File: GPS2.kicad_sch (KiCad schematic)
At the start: 12 parts, among them J3 GPS_ANT_2, U4 NEO-6M-GPS, U5 24AA32A-I_ST

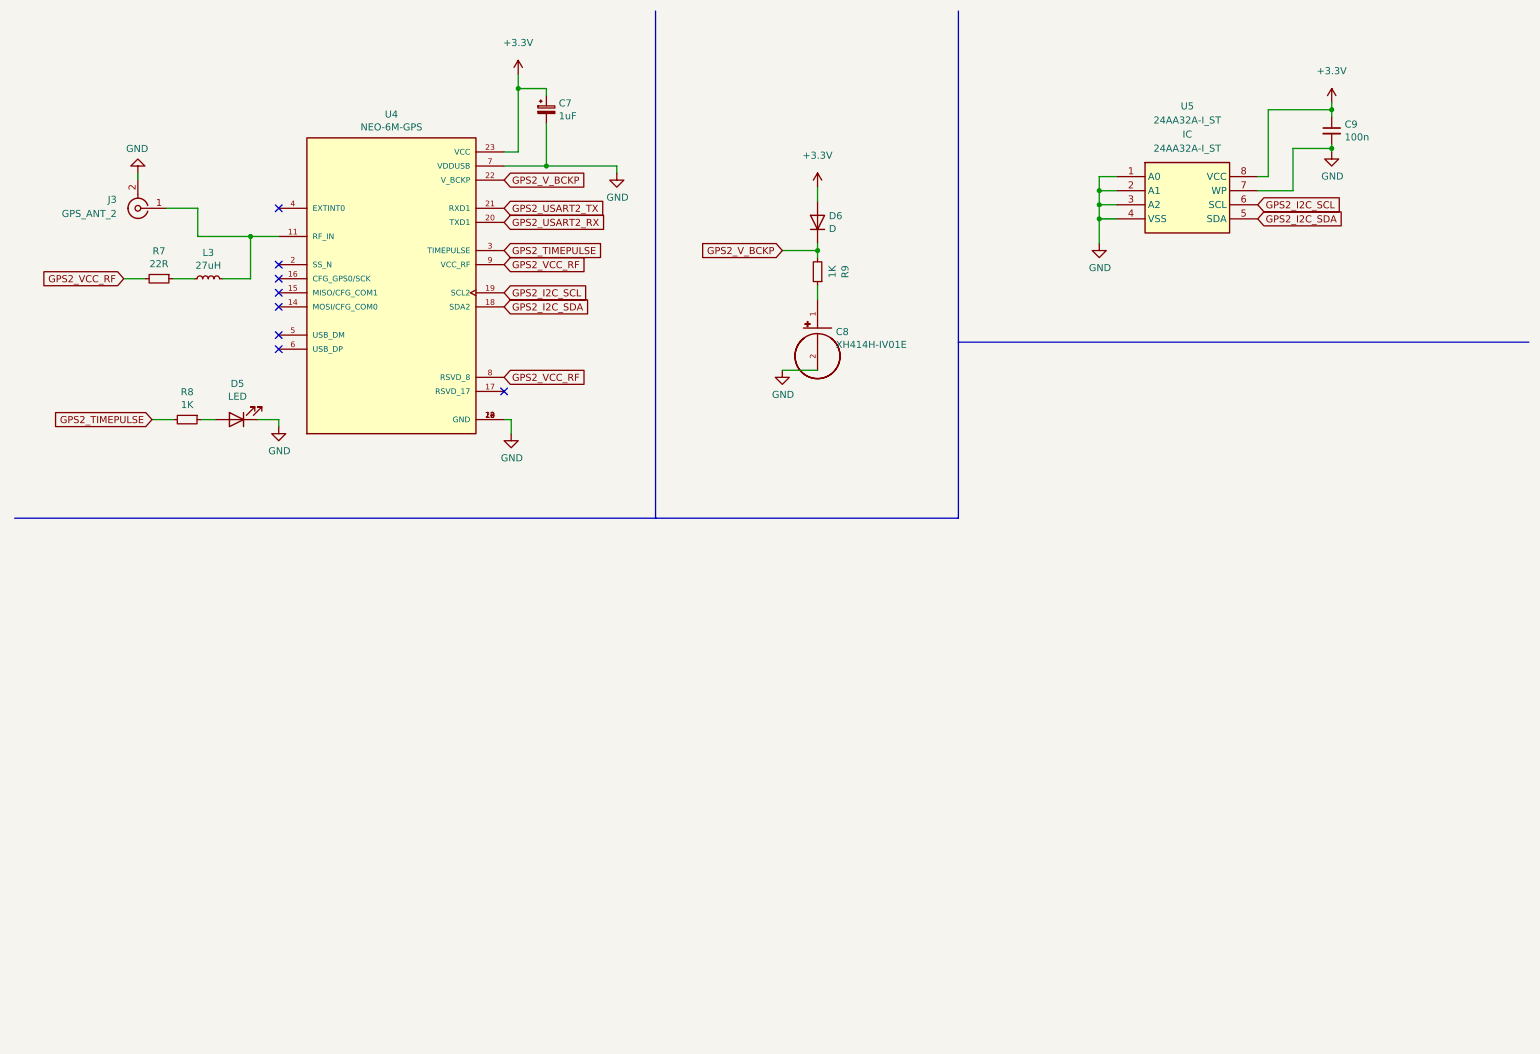
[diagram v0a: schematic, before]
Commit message: Adding M10
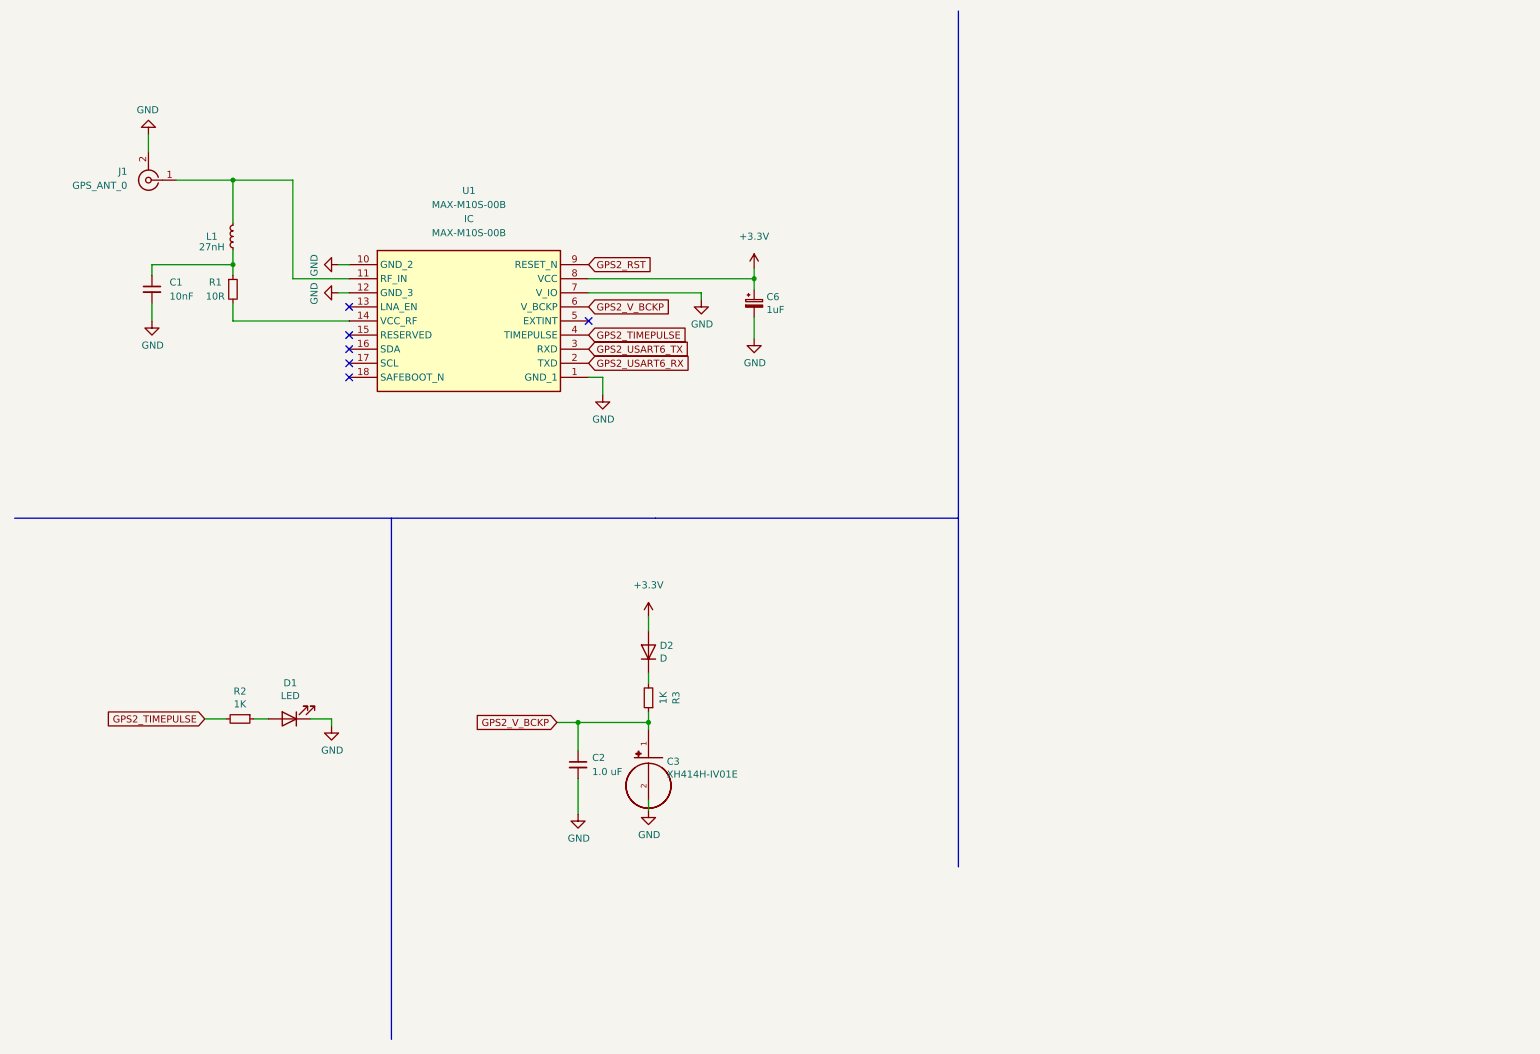
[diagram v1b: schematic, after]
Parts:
- removed C7: 1uF, Capacitor_Tantalum_SMD:CP_EIA-3528-21_Kemet-B_Pad1.50x2.35mm_HandSolder, symbol Device:CP_Small
- removed C8: XH414H-IV01E, XH414H:CAP_XH414H-IV01E, symbol XH414H-IV01E:XH414H-IV01E
- removed C9: 100n, Capacitor_SMD:C_0402_1005Metric, symbol Device:C_Small
- removed D5: LED, LED_SMD:LED_0805_2012Metric_Pad1.15x1.40mm_HandSolder, symbol Device:LED
- removed D6: D, Diode_SMD:D_1206_3216Metric_Pad1.42x1.75mm_HandSolder, symbol Device:D
- removed J3: GPS_ANT_2, Connector_Coaxial:SMA_Samtec_SMA-J-P-X-ST-EM1_EdgeMount, symbol Connector:Conn_Coaxial
- removed L3: 27uH, Inductor_SMD:L_0805_2012Metric, symbol Device:L_Small
- removed R7: 22R, Resistor_SMD:R_0805_2012Metric, symbol Device:R_Small
- removed R8, R9: 1K, Resistor_SMD:R_0805_2012Metric, symbol Device:R_Small
- removed U4: NEO-6M-GPS, NEO 6M:XCVR_NEO-6M-GPS, symbol NEO-6M-GPS:NEO-6M-GPS
- removed U5: 24AA32A-I_ST, 24AA32A-I_ST:SOP65P640X120-8N, symbol 24AA32A-I_ST:24AA32A-I_ST
- added C1: 10nF, Capacitor_SMD:C_0805_2012Metric, symbol Device:C_Small
- added C2: 1.0 uF, Capacitor_SMD:C_0805_2012Metric, symbol Device:C_Small
- added C3: XH414H-IV01E, XH414H:CAP_XH414H-IV01E, symbol XH414H-IV01E:XH414H-IV01E
- added C6: 1uF, Capacitor_Tantalum_SMD:CP_EIA-3528-21_Kemet-B_Pad1.50x2.35mm_HandSolder, symbol Device:CP_Small
- added D1: LED, LED_SMD:LED_0805_2012Metric_Pad1.15x1.40mm_HandSolder, symbol Device:LED
- added D2: D, Diode_SMD:D_1206_3216Metric_Pad1.42x1.75mm_HandSolder, symbol Device:D
- added J1: GPS_ANT_0, Connector_Coaxial:SMA_Samtec_SMA-J-P-X-ST-EM1_EdgeMount, symbol Connector:Conn_Coaxial
- added L1: 27nH, Inductor_SMD:L_0805_2012Metric, symbol Device:L_Small
- added R1: 10R, Resistor_SMD:R_0805_2012Metric, symbol Device:R_Small
- added R2, R3: 1K, Resistor_SMD:R_0805_2012Metric, symbol Device:R_Small
- added U1: MAX-M10S-00B, MAX-M10S-00B:MAXM10S00B, symbol MAX-M10S-00B:MAX-M10S-00B
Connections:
- net +3.3V: now also C6.1, D2.2 (A), U1.8 (VCC)
- net GND: now also C1.2, C2.2, C3.2, C6.2, D1.1 (K), J1.2 (Ext), U1.1 (GND_1), U1.10 (GND_2), U1.12 (GND_3), U1.7 (V_IO)
- net GPS2_TIMEPULSE: now also R2.2, U1.4 (TIMEPULSE)
- net GPS2_V_BCKP: now also C2.1, C3.1, R3.1, U1.6 (V_BCKP)
- new net: D1.2 (A), R2.1
- new net: J1.1 (In), L1.2, U1.11 (RF_IN)
- new net: R1.2, U1.14 (VCC_RF)
- new net: D2.1 (K), R3.2
- new net: C1.1, L1.1, R1.1
- new net GPS2_RST: U1.9 (RESET_N)
- new net GPS2_USART6_RX: U1.2 (TXD)
- new net GPS2_USART6_TX: U1.3 (RXD)
- no-connect marks 8 -> 6

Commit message: Finished M10
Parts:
- C1: footprint Capacitor_SMD:C_0805_2012Metric -> Capacitor_SMD:C_0402_1005Metric
- L1: footprint Inductor_SMD:L_0805_2012Metric -> Inductor_SMD:L_0402_1005Metric
- R1: footprint Resistor_SMD:R_0805_2012Metric -> Resistor_SMD:R_0402_1005Metric
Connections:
- net GPS2_RST renamed GPS2_RESET
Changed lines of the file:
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@@
+    )
+  )
+  (global_label "GPS2_RESET" (shape input) (at 115.57 57.785 0) (fields_autoplaced)
+    (effects (font (size 1.27 1.27)) (justify left))
+    (property "Intersheet References" "${INTERSHEET_REFS}" (id 0) (at 129.655 57.7056 0)
+      (effects (font (size 1.27 1.27)) (justify left) hide)
     )
   )
@@
     (effects (font (size 1.27 1.27)) (justify left))
     (property "Intersheet References" "${INTERSHEET_REFS}" (id 0) (at 134.1302 73.1044 0)
-      (effects (font (size 1.27 1.27)) (justify left) hide)
-    )
-  )
-  (global_label "GPS2_RST" (shape input) (at 115.57 57.785 0) (fields_autoplaced)
-    (effects (font (size 1.27 1.27)) (justify left))
-    (property "Intersheet References" "${INTERSHEET_REFS}" (id 0) (at 127.3569 57.7056 0)
       (effects (font (size 1.27 1.27)) (justify left) hide)
     )
@@
     (property "Reference" "L1" (id 0) (at 47.625 52.705 0))
     (property "Value" "27nH" (id 1) (at 47.625 54.61 0))
-    (property "Footprint" "Inductor_SMD:L_0805_2012Metric" (id 2) (at 51.435 52.705 0)
+    (property "Footprint" "Inductor_SMD:L_0402_1005Metric" (id 2) (at 51.435 52.705 0)
       (effects (font (size 1.27 1.27)) hide)
     )
@@
     (property "Reference" "R1" (id 0) (at 48.26 60.96 0))
     (property "Value" "10R" (id 1) (at 48.26 63.5 0))
-    (property "Footprint" "Resistor_SMD:R_0805_2012Metric" (id 2) (at 51.435 62.23 0)
+    (property "Footprint" "Resistor_SMD:R_0402_1005Metric" (id 2) (at 51.435 62.23 0)
       (effects (font (size 1.27 1.27)) hide)
     )
@@
       (effects (font (size 1.27 1.27)) (justify left))
     )
-    (property "Footprint" "Capacitor_SMD:C_0805_2012Metric" (id 2) (at 36.83 62.23 0)
-      (effects (font (size 1.27 1.27)) hide)
-    )
+    (property "Footprint" "Capacitor_SMD:C_0402_1005Metric" (id 2) (at 36.83 62.23 0)
+      (effects (font (size 1.27 1.27)) hide)
+    )

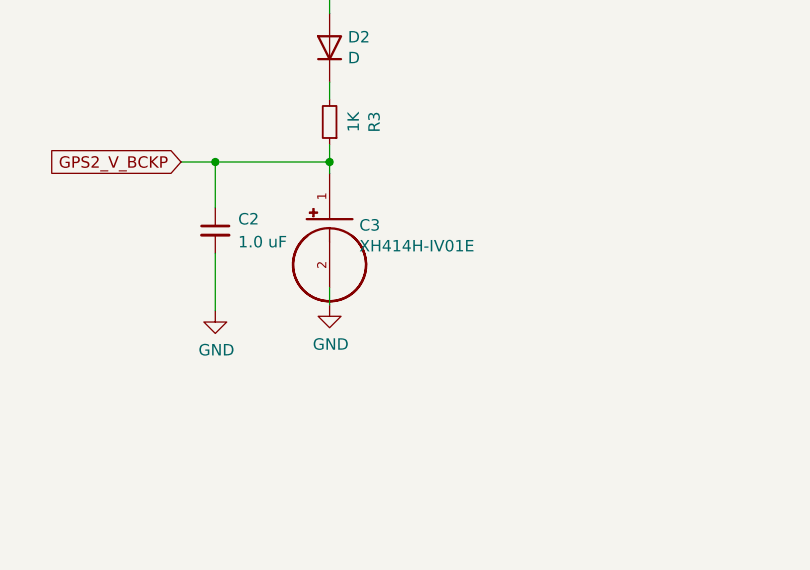
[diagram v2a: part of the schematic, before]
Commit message: Corrected battery position
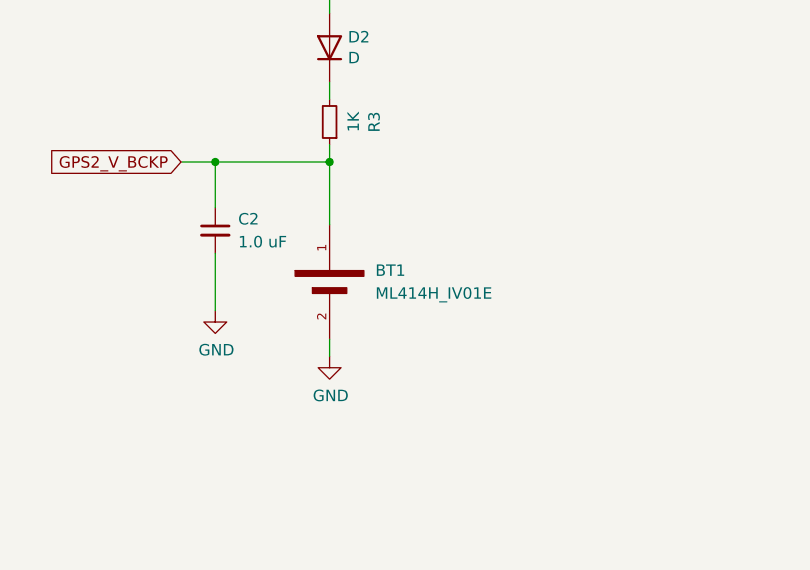
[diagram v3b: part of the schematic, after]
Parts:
- removed C3: XH414H-IV01E, XH414H:CAP_XH414H-IV01E, symbol XH414H-IV01E:XH414H-IV01E
- added BT1: ML414H_IV01E, ML414H_IV01E:SEIKO_ML414H_IV01E, symbol ML414H_IV01E:ML414H_IV01E
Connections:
- net GND: now also BT1.2
- net GPS2_V_BCKP: now also BT1.1
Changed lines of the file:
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@@
     (stroke (width 0) (type default) (color 0 0 0 0))
   )
-  (wire (pts (xy 126.365 154.305) (xy 126.365 156.21))
+  (wire (pts (xy 126.365 160.02) (xy 126.365 161.925))
     (stroke (width 0) (type default) (color 0 0 0 0))
   )
@@
     (stroke (width 0) (type default) (color 0 0 0 0))
   )
-  (wire (pts (xy 126.365 140.335) (xy 126.365 141.605))
+  (wire (pts (xy 126.365 140.335) (xy 126.365 147.32))
     (stroke (width 0) (type default) (color 0 0 0 0))
   )
@@
     )
     (pin "1")
+  )
+  (symbol (lib_id "ML414H_IV01E:ML414H_IV01E") (at 126.365 152.4 270) (unit 1)
+    (in_bom yes) (on_board yes) (fields_autoplaced)
+    (property "Reference" "BT1" (id 0) (at 131.445 152.3999 90)
+      (effects (font (size 1.27 1.27)) (justify left))
+    )
+    (property "Value" "ML414H_IV01E" (id 1) (at 131.445 154.9399 90)
+      (effects (font (size 1.27 1.27)) (justify left))
+    )
+    (property "Footprint" "ML414H_IV01E:SEIKO_ML414H_IV01E" (id 2) (at 126.365 152.4 0)
+      (effects (font (size 1.27 1.27)) (justify bottom) hide)
+    )
+    (property "Datasheet" "" (id 3) (at 126.365 152.4 0)
+      (effects (font (size 1.27 1.27)) hide)
+    )
+    (property "STANDARD" "Manufacturer Recommendation" (id 4) (at 126.365 152.4 0)
+      (effects (font (size 1.27 1.27)) (justify bottom) hide)
+    )
+    (property "MANUFACTURER" "SEIKO" (id 5) (at 126.365 152.4 0)
+      (effects (font (size 1.27 1.27)) (justify bottom) hide)
+    )
+    (pin "1")
+    (pin "2")
   )
   (symbol (lib_id "power:GND") (at 70.485 57.785 270) (unit 1)
@@
     (pin "2")
   )
-  (symbol (lib_id "power:GND") (at 126.365 156.21 0) (unit 1)
-    (in_bom yes) (on_board yes)
-    (property "Reference" "#PWR09" (id 0) (at 126.365 162.56 0)
-      (effects (font (size 1.27 1.27)) hide)
-    )
-    (property "Value" "GND" (id 1) (at 126.492 160.6042 0))
-    (property "Footprint" "" (id 2) (at 126.365 156.21 0)
-      (effects (font (size 1.27 1.27)) hide)
-    )
-    (property "Datasheet" "" (id 3) (at 126.365 156.21 0)
+  (symbol (lib_id "power:GND") (at 126.365 161.925 0) (unit 1)
+    (in_bom yes) (on_board yes)
+    (property "Reference" "#PWR09" (id 0) (at 126.365 168.275 0)
+      (effects (font (size 1.27 1.27)) hide)
+    )
+    (property "Value" "GND" (id 1) (at 126.492 166.3192 0))
+    (property "Footprint" "" (id 2) (at 126.365 161.925 0)
+      (effects (font (size 1.27 1.27)) hide)
+    )
+    (property "Datasheet" "" (id 3) (at 126.365 161.925 0)
       (effects (font (size 1.27 1.27)) hide)
     )
@@
     (pin "1")
   )
-  (symbol (lib_id "XH414H-IV01E:XH414H-IV01E") (at 126.365 146.685 0) (unit 1)
-    (in_bom yes) (on_board yes)
-    (property "Reference" "C3" (id 0) (at 129.667 147.3708 0)
-      (effects (font (size 1.27 1.27)) (justify left))
-    )
-    (property "Value" "XH414H-IV01E" (id 1) (at 129.667 149.6822 0)
-      (effects (font (size 1.27 1.27)) (justify left))
-    )
-    (property "Footprint" "XH414H:CAP_XH414H-IV01E" (id 2) (at 126.365 146.685 0)
-      (effects (font (size 1.27 1.27)) (justify left bottom) hide)
-    )
-    (property "Datasheet" "" (id 3) (at 126.365 146.685 0)
-      (effects (font (size 1.27 1.27)) (justify left bottom) hide)
-    )
-    (property "MANUFACTURER" "Seiko" (id 4) (at 126.365 146.685 0)
-      (effects (font (size 1.27 1.27)) (justify left bottom) hide)
-    )
-    (pin "1")
-    (pin "2")
-  )
   (symbol (lib_id "power:GND") (at 36.83 67.945 0) (unit 1)

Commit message: Last commit
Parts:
- removed D2: D, Diode_SMD:D_1206_3216Metric_Pad1.42x1.75mm_HandSolder, symbol Device:D
- added D2: B0520LW-7-F, B0520LW-7-F:SOD3716X145N, symbol B0520LW-7-F:B0520LW-7-F
- C6: value 1uF -> 10uF; footprint Capacitor_Tantalum_SMD:CP_EIA-3528-21_Kemet-B_Pad1.50x2.35mm_HandSolder -> Capacitor_SMD:C_1210_3225Metric
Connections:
- net +3.3V: now also U1.7 (V_IO), D2.2 (A)
- net GND: no longer U1.7 (V_IO)
- net at R3.2: now also D2.1 (K)
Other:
- moved on the sheet: BT1, C1, C2, C6, J1, L1, R1, R3, U1

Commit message: Second commit
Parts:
- removed C6: 10uF, Capacitor_SMD:C_1210_3225Metric, symbol Device:CP_Small
- removed D1: LED, LED_SMD:LED_0805_2012Metric_Pad1.15x1.40mm_HandSolder, symbol Device:LED
- removed D2: B0520LW-7-F, B0520LW-7-F:SOD3716X145N, symbol B0520LW-7-F:B0520LW-7-F
- removed U1: MAX-M10S-00B, MAX-M10S-00B:MAXM10S00B, symbol MAX-M10S-00B:MAX-M10S-00B
- added C26: 10uF, Capacitor_SMD:C_1210_3225Metric, symbol Device:C_Small
- added C27: 100n, Capacitor_SMD:C_0402_1005Metric, symbol Device:C_Small
- added C6: 1uF, Capacitor_SMD:C_1210_3225Metric, symbol Device:C_Small
- added D1: B0520LW-7-F, B0520LW-7-F:SOD3716X145N, symbol B0520LW-7-F:B0520LW-7-F
- added D2: LED, LED_SMD:LED_0805_2012Metric_Pad1.15x1.40mm_HandSolder, symbol Device:LED
- added IC3: 24AA32A-I_ST, 24AA32A-I_ST:SOP65P640X120-8N, symbol 24AA32A-I_ST:24AA32A-I_ST
- added R21: 10K, Resistor_SMD:R_0402_1005Metric, symbol Device:R_Small
- added R22, R23: 4.7K, Resistor_SMD:R_0402_1005Metric, symbol Device:R_Small
- added U1: NEO-M9N, NEO-M9N:XCVR_NEO-M9N, symbol NEO-M9N:NEO-M9N
- BT1: footprint ML414H_IV01E:SEIKO_ML414H_IV01E -> ML414H IV01E:SEIKO_ML414H_IV01E
- C1: value 10nF -> 1.0 uF; footprint Capacitor_SMD:C_0402_1005Metric -> Capacitor_SMD:C_0805_2012Metric
- C2: value 1.0 uF -> 100nF; footprint Capacitor_SMD:C_0805_2012Metric -> Capacitor_SMD:C_0402_1005Metric
- J1: footprint Connector_Coaxial:SMA_Samtec_SMA-J-P-X-ST-EM1_EdgeMount -> Connector_Coaxial:SMA_Samtec_SMA-J-P-H-ST-EM1_EdgeMount
- R1: value 10R -> 1K; footprint Resistor_SMD:R_0402_1005Metric -> Resistor_SMD:R_0805_2012Metric
- R2: value 1K -> 10R; footprint Resistor_SMD:R_0805_2012Metric -> Resistor_SMD:R_0402_1005Metric
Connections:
- net +3.3V: now also C26.1, C27.1, C6.1, D1.2 (A), IC3.8 (VCC), R21.2, R22.1, R23.1, U1.23 (VCC)
- net GND: now also C26.2, C27.2, C6.2, D2.1 (K), IC3.1 (A0), IC3.2 (A1), IC3.3 (A2), IC3.4 (VSS), IC3.7 (WP), U1.10 (GND), U1.12 (GND), U1.13 (GND), U1.24 (GND)
- net GPS2_RESET: now also U1.8 (RESET_N)
- net GPS2_TIMEPULSE: now also R3.2, U1.3 (TIMEPULSE); no longer R2.2
- net GPS2_USART6_RX: now also U1.20 (TXD/SPI_MISO)
- net GPS2_USART6_TX: now also U1.21 (RXD/SPI_MOSI)
- net GPS2_V_BCKP: now also C1.1, R1.1, U1.22 (V_BCKP); no longer C2.1, R3.1
- net at R2.1: now also C2.1, L1.1
- net at J1.1 (In), L1.2: now also U1.11 (RF_IN)
- net at R1.2: now also D1.1 (K)
- new net: D2.2 (A), R3.1
- new net: U1.15 (RESERVED), U1.16 (RESERVED), U1.17 (RESERVED)
- new net GPS2_D_SEL: R21.1, U1.2 (D_SEL)
- new net GPS2_I2C_SCL: IC3.6 (SCL), R23.2, U1.19 (SCL/SPI_CLK)
- new net GPS2_I2C_SDA: IC3.5 (SDA), R22.2, U1.18 (SDA/SPI_CS_N)
- new net GPS2_RF: R2.2, U1.9 (VCC_RF)
